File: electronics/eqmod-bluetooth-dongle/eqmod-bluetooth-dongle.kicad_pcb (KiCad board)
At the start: 2 copper layers, 45.2 x 23.6 mm, 6 parts, among them J1 Mount

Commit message: Power planes
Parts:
- moved J1 8.46 mm to (137.5, 91.9), turned to 0 degrees
- moved R1 8.38 mm to (140.8, 92.2), turned to -90 degrees
- moved R2 8.09 mm to (144.3, 102.4), turned to 90 degrees
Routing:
- net +5V: track 64.7 -> 2.51 mm
- net +3V3: track 38.2 -> 0.00 mm
- net MOUNT_TX: track 12.0 -> 5.97 mm
- net MOUNT_RX: track 9.37 -> 6.39 mm
- added copper zone on F.Cu, net +3V3
- added copper zone on F.Cu, net +5V

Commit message: With markings - ready to test
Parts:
- moved LM7805 0.55 mm to (137.5, 86.8)
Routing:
- net MOUNT_TX: track 5.97 -> 7.02 mm
- net MOUNT_+12V: track 8.42 -> 7.74 mm
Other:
- board size 45.2 x 23.6 mm -> 42.7 x 23.5 mm
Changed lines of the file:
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@@
 	(footprint "Package_TO_SOT_THT:TO-220-3_Vertical"
 		(layer "F.Cu")
-		(at 138 87)
+		(at 137.47 86.85)
 		(descr "TO-220-3, Vertical, RM 2.54mm, see https://www.vishay.com/docs/66542/to-220-1.pdf, generated with kicad-footprint-generator TO_SOT_THT_generate.py")
 		(tags "TO-220-3 Vertical RM 2.54mm")
@@
 		(at 109.5 94.85 180)
 		(property "Reference" "HC-05"
-			(at 2 0.1 270)
+			(at 2 0.1 90)
 			(layer "B.SilkS")
 			(effects
@@
 			(fill no)
 			(layer "B.Fab")
+		)
+		(fp_text user "TX"
+			(at -1.25 0.666666 0)
+			(unlocked yes)
+			(layer "B.SilkS")
+			(effects
+				(font
+					(size 0.8 0.8)
+					(thickness 0.1)
+				)
+				(justify right bottom mirror)
+			)
+		)
+		(fp_text user "+5V"
+			(at -1.25 -4.466667 0)
+			(unlocked yes)
+			(layer "B.SilkS")
+			(effects
+				(font
+					(size 0.8 0.8)
+					(thickness 0.1)
+				)
+				(justify right bottom mirror)
+			)
+		)
+		(fp_text user "RX"
+			(at -1.25 3.233333 0)
+			(unlocked yes)
+			(layer "B.SilkS")
+			(effects
+				(font
+					(size 0.8 0.8)
+					(thickness 0.1)
+				)
+				(justify right bottom mirror)
+			)
+		)
+		(fp_text user "GND"
+			(at -1.25 -1.9 0)
+			(unlocked yes)
+			(layer "B.SilkS")
+			(effects
+				(font
+					(size 0.8 0.8)
+					(thickness 0.1)
+				)
+				(justify right bottom mirror)
+			)
 		)
 		(pad "1" thru_hole rect
@@
 	)
 	(gr_arc
-		(start 107.83 106.284752)
-		(mid 106.415803 105.698963)
-		(end 105.83 104.284752)
+		(start 148.75 104.45)
+		(mid 148.164214 105.864214)
+		(end 146.75 106.45)
 		(stroke
 			(width 0.05)
@@
 		(layer "Edge.Cuts")
 	)
-	(gr_arc
-		(start 149.061847 82.703679)
-		(mid 150.476061 83.289465)
-		(end 151.061847 84.703679)
+	(gr_line
+		(start 108.05 82.95)
+		(end 146.75 82.95)
 		(stroke
 			(width 0.05)
@@
 		(layer "Edge.Cuts")
 	)
+	(gr_line
+		(start 106.05 104.45)
+		(end 106.05 84.95)
+		(stroke
+			(width 0.05)
+			(type default)
+		)
+		(layer "Edge.Cuts")
+	)
 	(gr_circle
-		(center 149.25 104.5)
-		(end 150.35 104.5)
+		(center 146.75 104.45)
+		(end 147.85 104.45)
 		(stroke
 			(width 0.05)
@@
 	)
 	(gr_line
-		(start 149.061847 106.284752)
-		(end 107.83 106.284752)
+		(start 146.75 106.45)
+		(end 108.05 106.45)
 		(stroke
 			(width 0.05)
@@
 	)
 	(gr_line
-		(start 151.061847 84.703679)
-		(end 151.061847 104.284752)
+		(start 148.75 84.95)
+		(end 148.75 104.45)
 		(stroke
 			(width 0.05)
@@
 		(layer "Edge.Cuts")
 	)
+	(gr_arc
+		(start 108.05 106.45)
+		(mid 106.635786 105.864214)
+		(end 106.05 104.45)
+		(stroke
+			(width 0.05)
+			(type default)
+		)
+		(layer "Edge.Cuts")
+	)
 	(gr_circle
-		(center 149.25 84.5)
-		(end 150.35 84.5)
+		(center 146.75 84.95)
+		(end 147.85 84.95)
 		(stroke
 			(width 0.05)
@@
 		(layer "Edge.Cuts")
 	)
-	(gr_line
-		(start 105.83 104.284752)
-		(end 105.83 84.703679)
+	(gr_circle
+		(center 108.05 104.45)
+		(end 109.15 104.45)
+		(stroke
+			(width 0.05)
+			(type solid)
+		)
+		(fill no)
+		(layer "Edge.Cuts")
+	)
+	(gr_arc
+		(start 106.05 84.95)
+		(mid 106.635786 83.535786)
+		(end 108.05 82.95)
 		(stroke
 			(width 0.05)
@@
 		(layer "Edge.Cuts")
 	)
-	(gr_arc
-		(start 105.83 84.703679)
-		(mid 106.415794 83.289479)
-		(end 107.83 82.703679)
-		(stroke
-			(width 0.05)
-			(type default)
-		)
-		(layer "Edge.Cuts")
-	)
 	(gr_circle
-		(center 107.9 104.5)
-		(end 109 104.5)
+		(center 108.05 84.95)
+		(end 109.15 84.95)
 		(stroke
 			(width 0.05)
@@
 		(layer "Edge.Cuts")
 	)
-	(gr_circle
-		(center 107.9 84.5)
-		(end 109 84.5)
-		(stroke
-			(width 0.05)
-			(type solid)
-		)
-		(fill no)
-		(layer "Edge.Cuts")
-	)
 	(gr_arc
-		(start 151.061847 104.284752)
-		(mid 150.476061 105.698966)
-		(end 149.061847 106.284752)
-		(stroke
-			(width 0.05)
-			(type default)
-		)
-		(layer "Edge.Cuts")
-	)
-	(gr_line
-		(start 107.83 82.703679)
-		(end 149.061847 82.703679)
+		(start 146.75 82.95)
+		(mid 148.164214 83.535786)
+		(end 148.75 84.95)
 		(stroke
 			(width 0.05)
@@
 	)
 	(segment
-		(start 139.96 87.45)
-		(end 139.91 87.5)
-		(width 0.2)
-		(layer "F.Cu")
-		(net 5)
-	)
-	(segment
 		(start 114.27 98.77)
 		(end 114.61 98.77)
@@
 	)
 	(segment
-		(start 146.25 104)
-		(end 146.58 104)
-		(width 0.2)
-		(layer "B.Cu")
-		(net 5)
-	)
-	(segment
 		(start 109.16 99)
 		(end 109.5 98.66)
@@
 	)
 	(segment
-		(start 137.04 94.1)
-		(end 135.7 94.1)
+		(start 137.46 94.4)
+		(end 137.5 94.4)
 		(width 0.4)
 		(layer "F.Cu")
@@
 	)
 	(segment
-		(start 135.7 94.1)
-		(end 132.75 91.15)
-		(width 0.4)
-		(layer "F.Cu")
-		(net 7)
-	)
-	(segment
-		(start 132.75 91.15)
+		(start 133.4 91.15)
 		(end 132.38 91.15)
 		(width 0.4)
@@
 	)
 	(segment
+		(start 137.5 94.4)
+		(end 136.65 94.4)
+		(width 0.4)
+		(layer "F.Cu")
+		(net 7)
+	)
+	(segment
+		(start 136.65 94.4)
+		(end 133.4 91.15)
+		(width 0.4)
+		(layer "F.Cu")
+		(net 7)
+	)
+	(segment
 		(start 137.1 94.04)
-		(end 137.04 94.1)
+		(end 137.46 94.4)
 		(width 0.4)
 		(layer "F.Cu")
@@
 	)
 	(segment
-		(start 137.1 91.5)
-		(end 138.95 89.65)
+		(start 137.5 91.86)
+		(end 139.56 89.8)
 		(width 0.4)
 		(layer "F.Cu")
@@
 	)
 	(segment
-		(start 138.95 89.65)
-		(end 140.43 89.65)
+		(start 142.55 87.75)
+		(end 142.55 86.85)
 		(width 0.4)
 		(layer "F.Cu")
@@
 	)
 	(segment
-		(start 143.08 87)
-		(end 143.08 87.58)
-		(width 0.2)
+		(start 140.5 89.8)
+		(end 142.55 87.75)
+		(width 0.4)
 		(layer "F.Cu")
 		(net 8)
 	)
 	(segment
-		(start 140.43 89.65)
-		(end 143.08 87)
+		(start 139.56 89.8)
+		(end 140.5 89.8)
 		(width 0.4)
 		(layer "F.Cu")
@@
 	)
 	(segment
-		(start 137.1 96.58)
-		(end 137.03 96.65)
+		(start 137.56 91.8)
+		(end 137.5 91.86)
 		(width 0.4)
 		(layer "F.Cu")
-		(net 9)
-	)
-	(segment
-		(start 135.7 96.65)
-		(end 132.74 93.69)
-		(width 0.4)
-		(layer "F.Cu")
-		(net 9)
+		(net 8)
 	)
 	(segment
@@
 	)
 	(segment
-		(start 137.03 96.65)
-		(end 135.7 96.65)
+		(start 132.39 93.69)
+		(end 133.44 93.69)
 		(width 0.4)
 		(layer "F.Cu")
@@
 	)
 	(segment
-		(start 132.81 93.69)
-		(end 132.39 93.69)
-		(width 0.2)
+		(start 133.44 93.69)
+		(end 136.69 96.94)
+		(width 0.4)
+		(layer "F.Cu")
+		(net 9)
+	)
+	(segment
+		(start 136.69 96.94)
+		(end 137.5 96.94)
+		(width 0.4)
 		(layer "F.Cu")
 		(net 9)
@@
 		(polygon
 			(pts
-				(xy 151.55 107.25) (xy 151.6 98.95) (xy 127.75 98.75) (xy 118.45 88.65) (xy 111.715231 88.65) (xy 111.45 106.85)
-				(xy 105.25 106.85) (xy 105.5 81.2) (xy 151.65 81.7)
+				(xy 149.75 98.95) (xy 149.75 98.95) (xy 127.75 98.75) (xy 118.45 88.65) (xy 111.715231 88.65) (xy 111.45 107.3)
+				(xy 105.15 107.3) (xy 105.5 82) (xy 149.65 81.95)
 			)
 		)
@@
 		(polygon
 			(pts
-				(xy 111.45 106.85) (xy 111.715231 88.65) (xy 118.45 88.65) (xy 127.75 98.75) (xy 151.6 98.95) (xy 151.55 107.25)
+				(xy 111.45 107.3) (xy 111.715231 88.65) (xy 118.45 88.65) (xy 127.75 98.75) (xy 149.75 98.95) (xy 149.85 107.35)
 			)
 		)
@@
 		(polygon
 			(pts
-				(xy 105.75 106.25) (xy 105.75 82.5) (xy 151 82.75) (xy 151 106.25)
-			)
-		)
+				(xy 105.85 107.05) (xy 105.8 82.45) (xy 149.05 82.3) (xy 149.3 107)
+			)
+		)

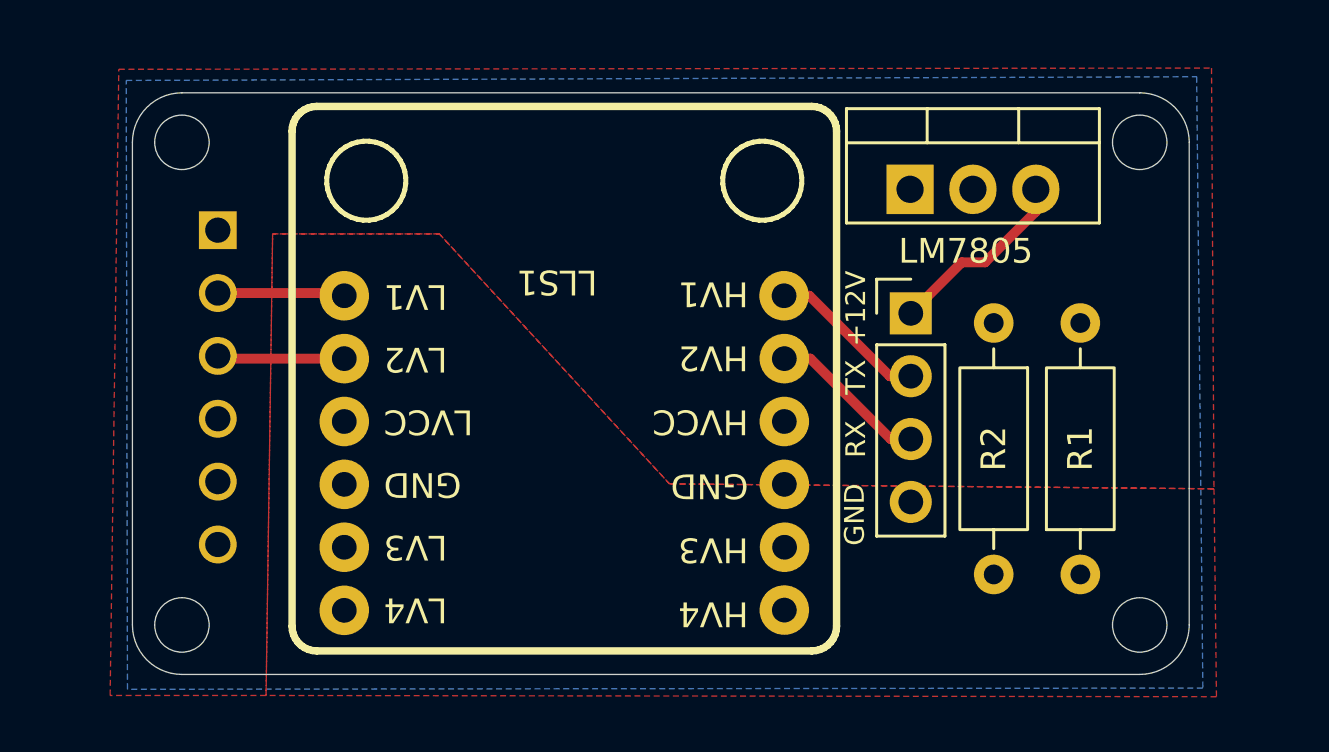
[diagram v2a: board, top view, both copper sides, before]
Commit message: 4-layer PCB and documentation
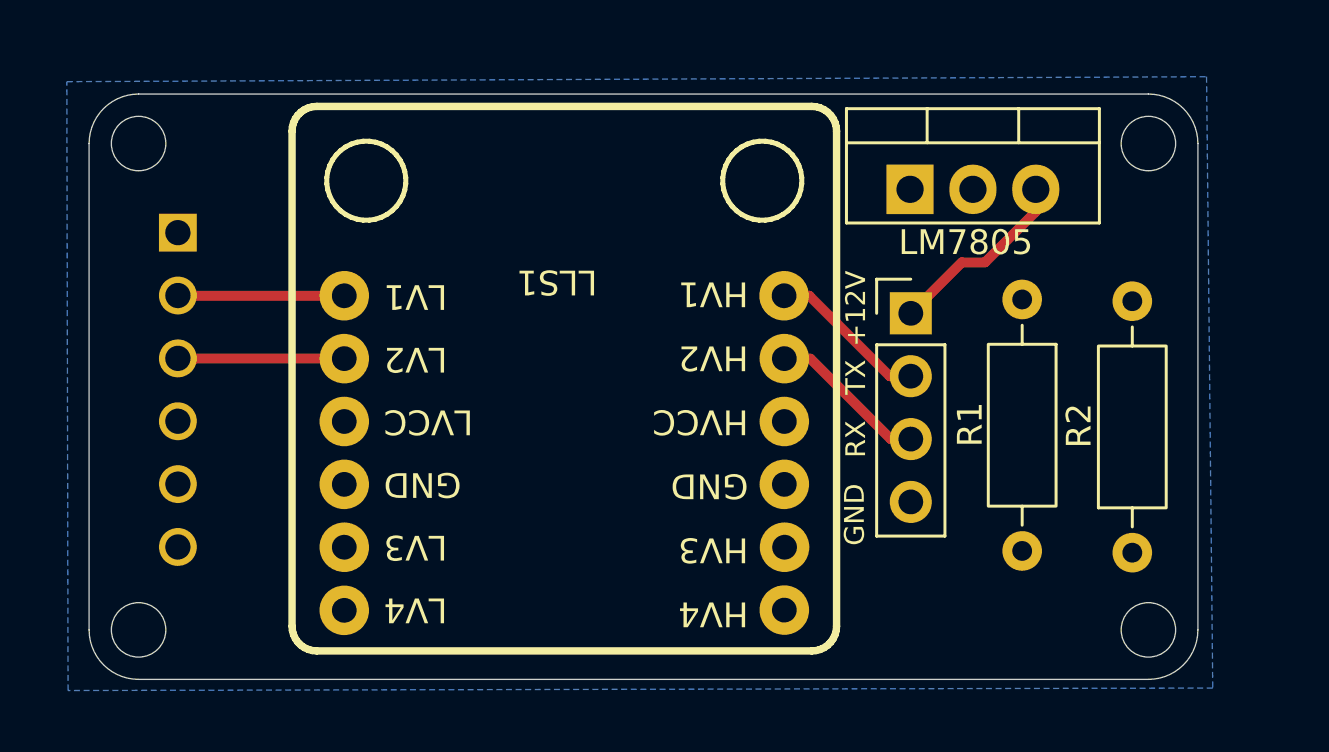
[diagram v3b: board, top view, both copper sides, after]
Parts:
- moved R2 2.28 mm to (146.4, 101.5)
- moved HC-05 1.62 mm to (107.9, 95.0)
- moved R1 1.49 mm to (142.0, 91.3)
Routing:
- net Net-(HC-05-RX): track 5.21 -> 6.98 mm
- net Net-(HC-05-TX): track 5.16 -> 6.73 mm
- net +5V: track 2.51 -> 1.69 mm
- added copper zone on In1.Cu, net +3V3
- added copper zone on In2.Cu, net +5V
- removed copper zone on F.Cu, net +3V3
- removed copper zone on F.Cu, net +5V
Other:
- board size 42.7 x 23.5 mm -> 44.8 x 23.7 mm
- copper layers 2 -> 4
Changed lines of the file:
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@@
 	(layers
 		(0 "F.Cu" signal)
+		(4 "In1.Cu" signal)
+		(6 "In2.Cu" signal)
 		(2 "B.Cu" signal)
 		(9 "F.Adhes" user "F.Adhesive")
@@
 	)
 	(setup
+		(stackup
+			(layer "F.SilkS"
+				(type "Top Silk Screen")
+			)
+			(layer "F.Paste"
+				(type "Top Solder Paste")
+			)
+			(layer "F.Mask"
+				(type "Top Solder Mask")
+				(thickness 0.01)
+			)
+			(layer "F.Cu"
+				(type "copper")
+				(thickness 0.035)
+			)
+			(layer "dielectric 1"
+				(type "prepreg")
+				(thickness 0.1)
+				(material "FR4")
+				(epsilon_r 4.5)
+				(loss_tangent 0.02)
+			)
+			(layer "In1.Cu"
+				(type "copper")
+				(thickness 0.035)
+			)
+			(layer "dielectric 2"
+				(type "core")
+				(thickness 1.24)
+				(material "FR4")
+				(epsilon_r 4.5)
+				(loss_tangent 0.02)
+			)
+			(layer "In2.Cu"
+				(type "copper")
+				(thickness 0.035)
+			)
+			(layer "dielectric 3"
+				(type "prepreg")
+				(thickness 0.1)
+				(material "FR4")
+				(epsilon_r 4.5)
+				(loss_tangent 0.02)
+			)
+			(layer "B.Cu"
+				(type "copper")
+				(thickness 0.035)
+			)
+			(layer "B.Mask"
+				(type "Bottom Solder Mask")
+				(thickness 0.01)
+			)
+			(layer "B.Paste"
+				(type "Bottom Solder Paste")
+			)
+			(layer "B.SilkS"
+				(type "Bottom Silk Screen")
+			)
+			(copper_finish "None")
+			(dielectric_constraints no)
+		)
 		(pad_to_mask_clearance 0)
 		(allow_soldermask_bridges_in_footprints no)
@@
 		(tags "TO-220-3 Vertical RM 2.54mm")
 		(property "Reference" "LM7805"
-			(at 2.25 2.5 0)
+			(at 2.25 2.15 0)
 			(layer "F.SilkS")
 			(effects
@@
 	(footprint "Resistor_THT:R_Axial_DIN0207_L6.3mm_D2.5mm_P10.16mm_Horizontal"
 		(layer "F.Cu")
-		(at 144.35 102.41 90)
+		(at 146.45 101.53 90)
 		(descr "Resistor, Axial_DIN0207 series, Axial, Horizontal, pin pitch=10.16mm, 0.25W = 1/4W, length*diameter=6.3*2.5mm^2, http://cdn-reichelt.de/documents/datenblatt/B400/1_4W%23YAG.pdf")
 		(tags "Resistor Axial_DIN0207 series Axial Horizontal pin pitch 10.16mm 0.25W = 1/4W length 6.3mm diameter 2.5mm")
 		(property "Reference" "R2"
-			(at 5.08 -3.5 90)
+			(at 5.13 -2.15 90)
 			(layer "F.SilkS")
 			(effects
@@
 	(footprint "Resistor_THT:R_Axial_DIN0207_L6.3mm_D2.5mm_P10.16mm_Horizontal"
 		(layer "F.Cu")
-		(at 140.85 92.25 -90)
+		(at 142 91.3 -90)
 		(descr "Resistor, Axial_DIN0207 series, Axial, Horizontal, pin pitch=10.16mm, 0.25W = 1/4W, length*diameter=6.3*2.5mm^2, http://cdn-reichelt.de/documents/datenblatt/B400/1_4W%23YAG.pdf")
 		(tags "Resistor Axial_DIN0207 series Axial Horizontal pin pitch 10.16mm 0.25W = 1/4W length 6.3mm diameter 2.5mm")
 		(property "Reference" "R1"
-			(at 5.08 -3.5 90)
+			(at 5.05 2.1 90)
 			(layer "F.SilkS")
 			(effects
@@
 	(footprint "ZC142200:MODULE_ZC142200_HC05"
 		(layer "B.Cu")
-		(at 109.5 94.85 180)
+		(at 107.8875 94.95 180)
 		(property "Reference" "HC-05"
 			(at 2 0.1 90)
@@
 		(embedded_fonts no)
 	)
-	(gr_arc
-		(start 148.75 104.45)
-		(mid 148.164214 105.864214)
-		(end 146.75 106.45)
+	(gr_line
+		(start 106.3 83)
+		(end 147.1 83)
 		(stroke
 			(width 0.05)
@@
 		(layer "Edge.Cuts")
 	)
-	(gr_line
-		(start 108.05 82.95)
-		(end 146.75 82.95)
+	(gr_circle
+		(center 147.1 104.65)
+		(end 148.2 104.65)
+		(stroke
+			(width 0.05)
+			(type solid)
+		)
+		(fill no)
+		(layer "Edge.Cuts")
+	)
+	(gr_arc
+		(start 106.3 106.65)
+		(mid 104.885786 106.064214)
+		(end 104.3 104.65)
 		(stroke
 			(width 0.05)
@@
 	)
 	(gr_line
-		(start 106.05 104.45)
-		(end 106.05 84.95)
+		(start 104.3 104.65)
+		(end 104.3 85)
 		(stroke
 			(width 0.05)
@@
 		(layer "Edge.Cuts")
 	)
-	(gr_circle
-		(center 146.75 104.45)
-		(end 147.85 104.45)
+	(gr_line
+		(start 147.1 106.65)
+		(end 106.3 106.65)
 		(stroke
 			(width 0.05)
-			(type solid)
+			(type default)
 		)
-		(fill no)
 		(layer "Edge.Cuts")
 	)
-	(gr_line
-		(start 146.75 106.45)
-		(end 108.05 106.45)
+	(gr_arc
+		(start 149.1 104.65)
+		(mid 148.514214 106.064214)
+		(end 147.1 106.65)
 		(stroke
 			(width 0.05)
@@
 		(layer "Edge.Cuts")
 	)
-	(gr_line
-		(start 148.75 84.95)
-		(end 148.75 104.45)
+	(gr_arc
+		(start 147.1 83)
+		(mid 148.514214 83.585786)
+		(end 149.1 85)
 		(stroke
 			(width 0.05)
@@
 	)
 	(gr_arc
-		(start 108.05 106.45)
-		(mid 106.635786 105.864214)
-		(end 106.05 104.45)
+		(start 104.3 85)
+		(mid 104.885786 83.585786)
+		(end 106.3 83)
 		(stroke
 			(width 0.05)
@@
 	)
 	(gr_circle
-		(center 146.75 84.95)
-		(end 147.85 84.95)
+		(center 147.1 85)
+		(end 148.2 85)
 		(stroke
 			(width 0.05)
@@
 	)
 	(gr_circle
-		(center 108.05 104.45)
-		(end 109.15 104.45)
+		(center 106.3 104.65)
+		(end 107.4 104.65)
 		(stroke
 			(width 0.05)
@@
 		(layer "Edge.Cuts")
 	)
-	(gr_arc
-		(start 106.05 84.95)
-		(mid 106.635786 83.535786)
-		(end 108.05 82.95)
+	(gr_line
+		(start 149.1 85)
+		(end 149.1 104.65)
 		(stroke
 			(width 0.05)
@@
 	)
 	(gr_circle
-		(center 108.05 84.95)
-		(end 109.15 84.95)
+		(center 106.3 85)
+		(end 107.4 85)
 		(stroke
 			(width 0.05)
@@
 		(layer "Edge.Cuts")
 	)
-	(gr_arc
-		(start 146.75 82.95)
-		(mid 148.164214 83.535786)
-		(end 148.75 84.95)
-		(stroke
-			(width 0.05)
-			(type default)
-		)
-		(layer "Edge.Cuts")
-	)
 	(gr_text "GND"
 		(at 116.2 98.196 180)
@@
 	(segment
 		(start 114.61 93.69)
-		(end 109.61 93.69)
+		(end 107.8975 93.69)
 		(width 0.4)
 		(layer "F.Cu")
@@
 	)
 	(segment
-		(start 109.61 93.69)
-		(end 109.5 93.58)
-		(width 0.2)
+		(start 107.8975 93.69)
+		(end 107.8875 93.68)
+		(width 0.4)
 		(layer "F.Cu")
 		(net 3)
@@
 	)
 	(segment
-		(start 114.46 91.04)
-		(end 109.5 91.04)
+		(start 114.61 91.15)
+		(end 107.8975 91.15)
 		(width 0.4)
 		(layer "F.Cu")
@@
 	)
 	(segment
+		(start 107.8975 91.15)
+		(end 107.8875 91.14)
+		(width 0.2)
+		(layer "F.Cu")
+		(net 4)
+	)
+	(segment
 		(start 114.27 98.77)
 		(end 114.61 98.77)
@@
 	)
 	(segment
-		(start 109.16 99)
-		(end 109.5 98.66)
-		(width 0.2)
-		(layer "F.Cu")
-		(net 6)
-	)
-	(segment
 		(start 132.39 96.23)
 		(end 132.98 96.23)
@@
 	)
 	(segment
-		(start 109.16 98.66)
-		(end 109.16 99)
-		(width 0.2)
-		(layer "F.Cu")
-		(net 6)
-	)
-	(segment
 		(start 137.46 94.4)
 		(end 137.5 94.4)
@@
 	)
 	(zone
-		(net 6)
-		(net_name "+5V")
-		(layer "F.Cu")
+		(net 5)
+		(net_name "GND")
+		(layer "B.Cu")
 		(hatch edge 0.5)
-		(priority 2)
 		(connect_pads
 			(clearance 0.5)
@@
 		(polygon
 			(pts
-				(xy 149.75 98.95) (xy 149.75 98.95) (xy 127.75 98.75) (xy 118.45 88.65) (xy 111.715231 88.65) (xy 111.45 107.3)
-				(xy 105.15 107.3) (xy 105.5 82) (xy 149.65 81.95)
+				(xy 103.45 107.1) (xy 103.4 82.5) (xy 149.45 82.3) (xy 149.7 107)
 			)
 		)
@@
 		(net 11)
 		(net_name "+3V3")
-		(layer "F.Cu")
+		(layer "In1.Cu")
 		(hatch edge 0.5)
 		(priority 1)
@@
 		(polygon
 			(pts
-				(xy 111.45 107.3) (xy 111.715231 88.65) (xy 118.45 88.65) (xy 127.75 98.75) (xy 149.75 98.95) (xy 149.85 107.35)
+				(xy 102.9 82.1) (xy 150.25 81.85) (xy 150.4 107.4) (xy 102.9 107.65)
 			)
 		)
 	)
 	(zone
-		(net 5)
-		(net_name "GND")
-		(layer "B.Cu")
+		(net 6)
+		(net_name "+5V")
+		(layer "In2.Cu")
 		(hatch edge 0.5)
+		(priority 2)
 		(connect_pads
 			(clearance 0.5)
@@
 		(polygon
 			(pts
-				(xy 105.85 107.05) (xy 105.8 82.45) (xy 149.05 82.3) (xy 149.3 107)
+				(xy 102.3 81.45) (xy 151 81.3) (xy 151.05 108.05) (xy 102.3 108.05)
 			)
 		)

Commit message: Change mount connector to standard JST connector
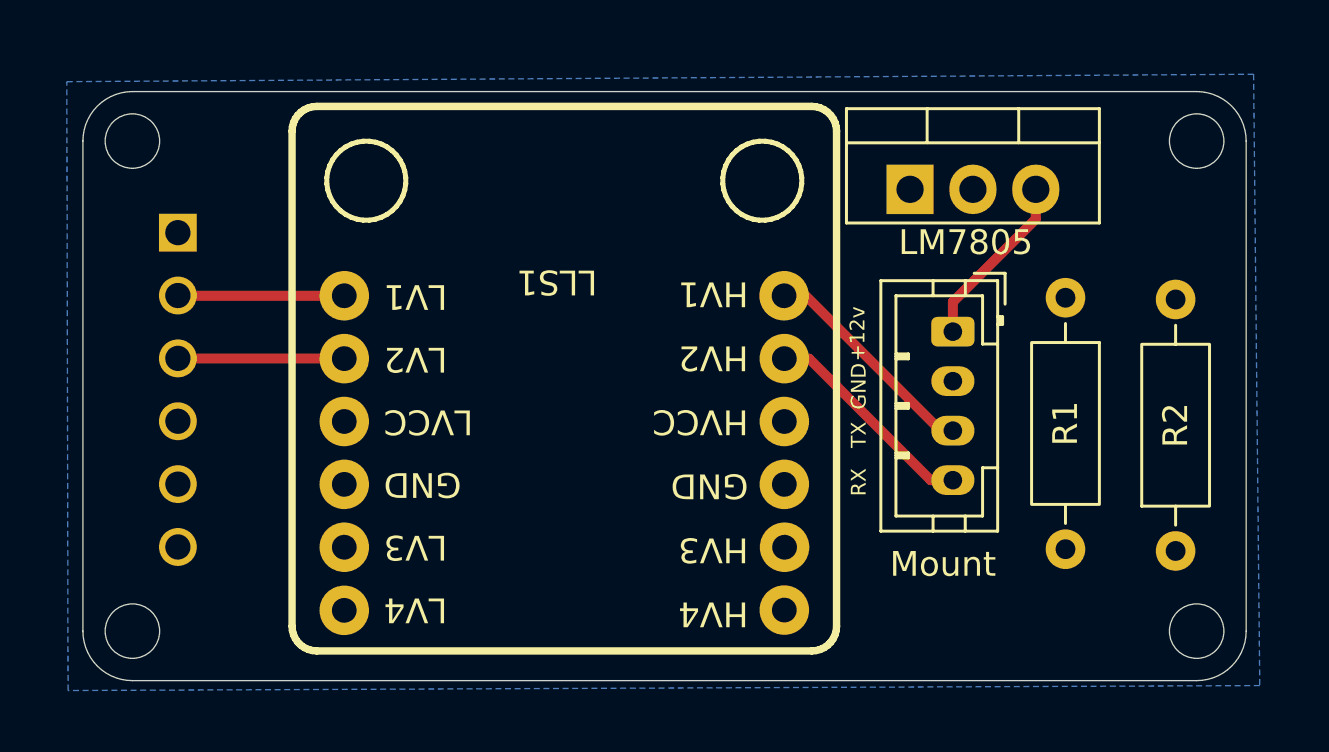
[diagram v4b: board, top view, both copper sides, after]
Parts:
- Mount: renamed from J1; footprint Connector_PinHeader_2.54mm:PinHeader_1x04_P2.54mm_Vertical -> Connector_JST:JST_PH_B4B-PH-K_1x04_P2.00mm_Vertical
- moved Mount 1.85 mm to (139.2, 92.6), turned to -90 degrees
- moved R2 1.75 mm to (148.2, 101.5)
- moved R1 1.75 mm to (143.8, 91.2)
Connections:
- Mount pad 2: MOUNT_TX -> GND
- Mount pad 3: MOUNT_RX -> MOUNT_TX
- Mount pad 4: GND -> MOUNT_RX
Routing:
- net MOUNT_TX: track 7.02 -> 9.82 mm
- net MOUNT_RX: track 6.81 -> 8.84 mm
- net MOUNT_+12V: track 7.74 -> 8.74 mm
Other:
- board size 44.8 x 23.7 mm -> 47 x 23.8 mm
